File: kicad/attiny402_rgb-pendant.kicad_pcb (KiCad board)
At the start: 2 copper layers, 40.6 x 25.4 mm, 5 parts, among them J1 Conn_01x03_Male, U1 ATtiny402-SS

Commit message: Update KiCad files to version 6
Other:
- net class Default removed

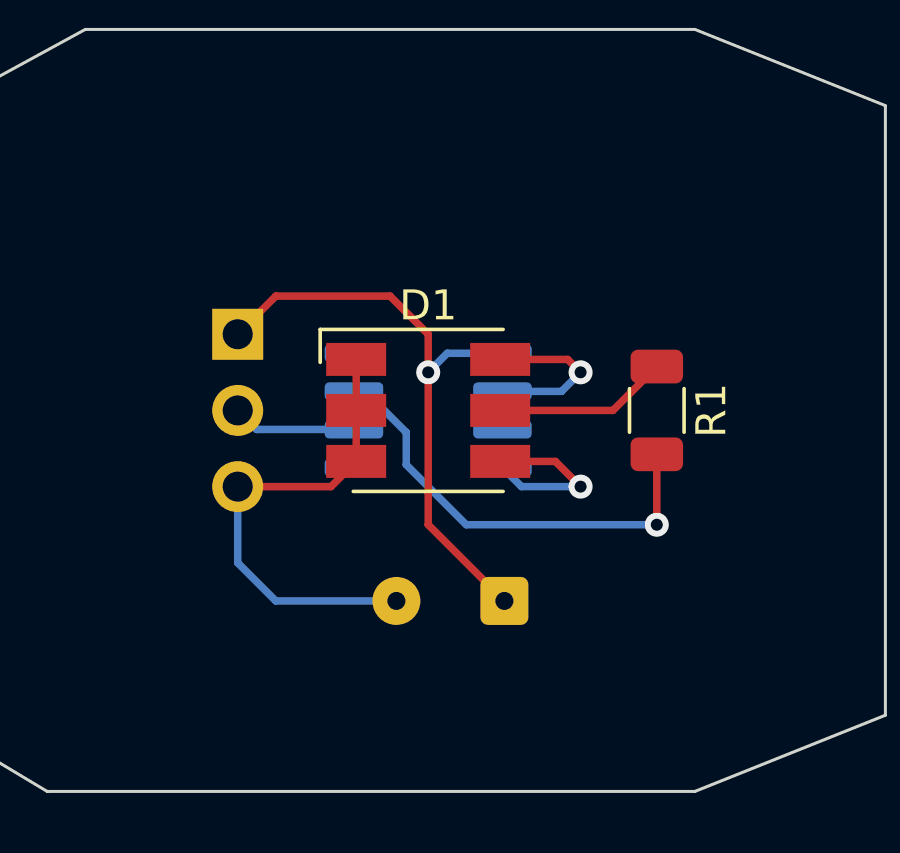
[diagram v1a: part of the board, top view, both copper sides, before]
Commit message: Added extra 1 ohm resistors on blue and green lines
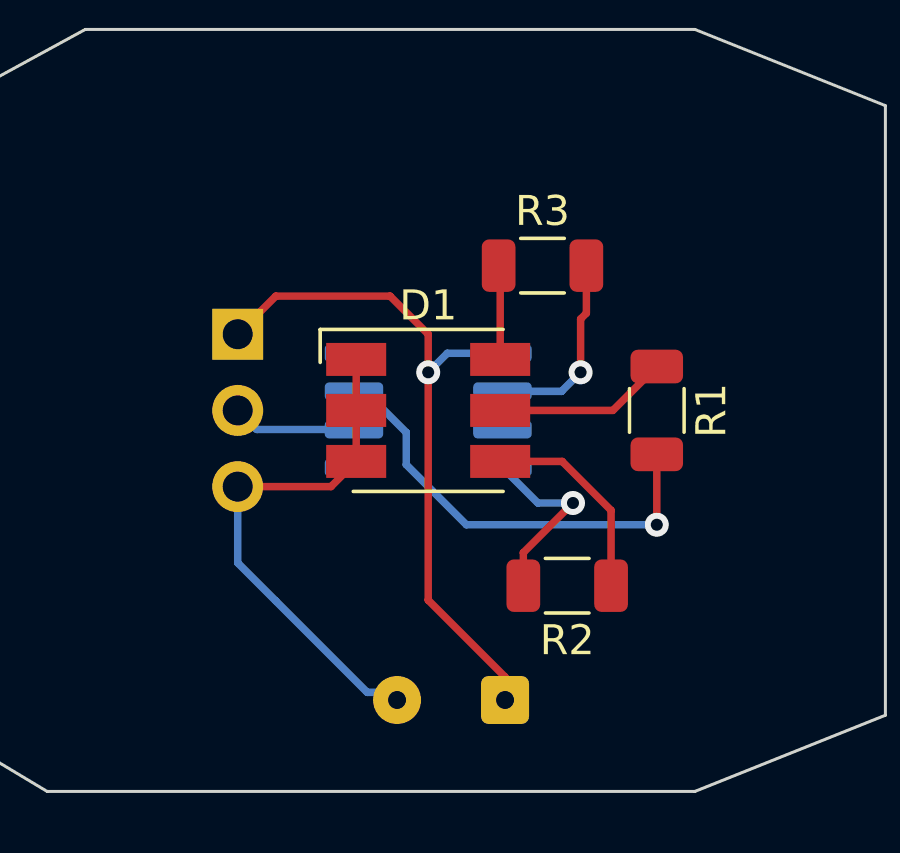
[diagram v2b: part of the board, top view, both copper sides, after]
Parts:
- added R2: 1, Resistor_SMD:R_1206_3216Metric, F.Cu at (153.2, 98.6)
- added R3: 1, Resistor_SMD:R_1206_3216Metric, F.Cu at (152.4, 87.9)
- moved BT1 3.30 mm to (151.2, 102.4)
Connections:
- D1 pad 4: /GREEN -> Net-(D1-Pad4)
- D1 pad 6: /BLUE -> Net-(D1-Pad6)
- U1 pad 3: Net-(U1-Pad3) -> unconnected-(U1-Pad3)
- U1 pad 5: Net-(U1-Pad5) -> unconnected-(U1-Pad5)
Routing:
- net Net-(D1-Pad4): track 0.00 -> 6.88 mm
- net Net-(D1-Pad6): track 0.00 -> 3.48 mm
- net +3V0: track 20.1 -> 23.4 mm
- net GND: track 16.1 -> 17.4 mm

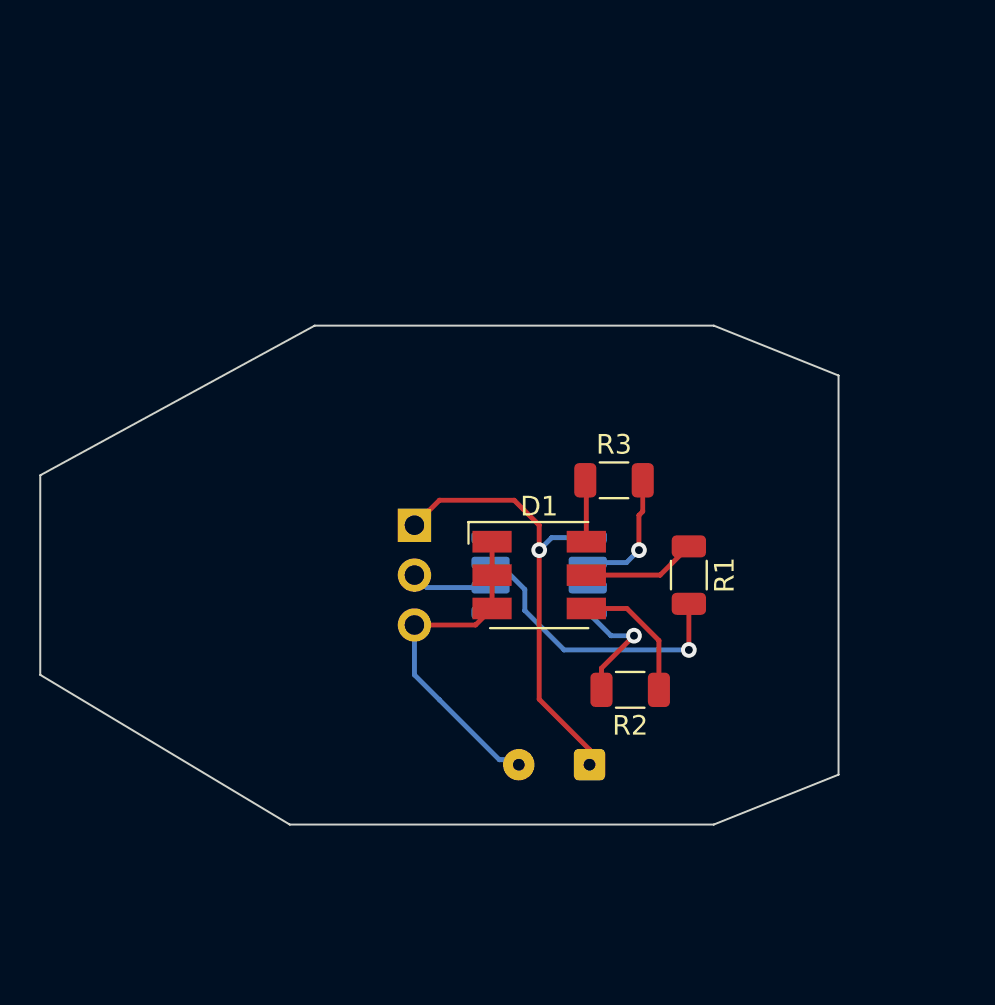
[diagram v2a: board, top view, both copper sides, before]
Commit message: One-sided PCB for hand-etching
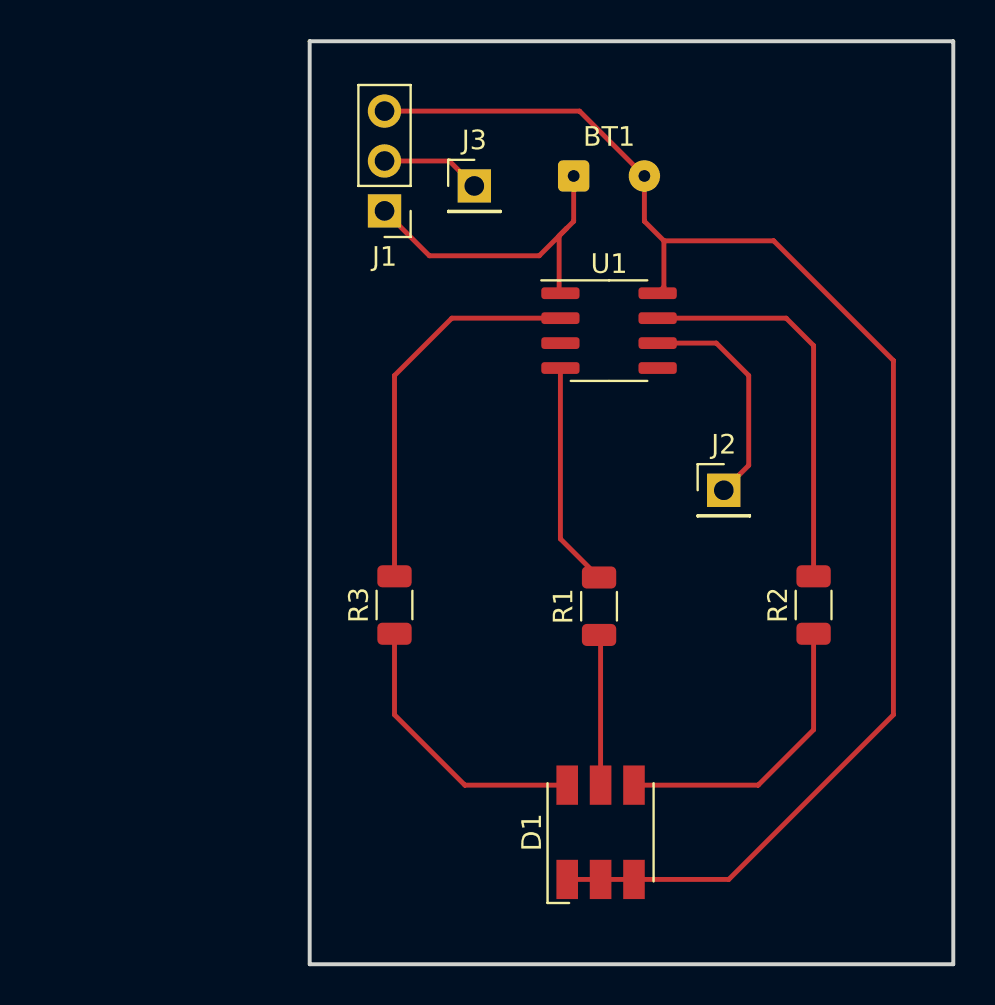
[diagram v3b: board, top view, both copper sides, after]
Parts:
- added J2: Conn_01x01_Male, Connector_PinHeader_2.54mm:PinHeader_1x01_P2.54mm_Vertical, F.Cu at (158.0, 88.4)
- added J3: Conn_01x01_Male, Connector_PinHeader_2.54mm:PinHeader_1x01_P2.54mm_Vertical, F.Cu at (145.3, 72.9)
- BT1, U1: moved to F.Cu
- J1: footprint Connector_PinHeader_2.54mm:PinHeader_1x03_P2.54mm_Horizontal -> Connector_PinHeader_2.54mm:PinHeader_1x03_P2.54mm_Vertical; moved to F.Cu
- moved BT1 30.0 mm to (150.3, 72.4), turned to 0 degrees
- moved J1 16.1 mm to (140.7, 74.2)
- moved D1 13.5 mm to (151.7, 105.8), turned to 90 degrees
- moved U1 12.9 mm to (152.1, 80.3), turned to 0 degrees
- moved R3 12.9 mm to (141.2, 94.2), turned to 90 degrees
- moved R2 10.3 mm to (162.6, 94.2), turned to 90 degrees
- moved R1 4.84 mm to (151.6, 94.3), turned to 90 degrees
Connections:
- J1 pad 2: /UPDI -> Net-(J1-Pad2)
- U1 pad 4: /GREEN -> /RED
- U1 pad 7: /RED -> /GREEN
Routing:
- net GND: track 17.4 -> 73.4 mm
- net /GREEN: track 6.98 -> 20.3 mm, vias 1 -> 0
- net /BLUE: track 6.63 -> 19.9 mm, vias 1 -> 0
- net Net-(D1-Pad6): track 3.48 -> 14.4 mm
- net Net-(D1-Pad4): track 6.88 -> 15.2 mm
- net /UPDI: track 4.14 -> 11.7 mm
- net +3V0: track 23.4 -> 17.1 mm, vias 1 -> 0
- net Net-(J1-Pad2): track 0.00 -> 5.10 mm
- net /RED: track 15.5 -> 11.5 mm, vias 1 -> 0
- net Net-(D1-Pad5): track 5.83 -> 7.68 mm
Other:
- board size 40.6 x 25.4 mm -> 32.8 x 47 mm
